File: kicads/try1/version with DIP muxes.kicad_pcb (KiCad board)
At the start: 2 copper layers, 166.5 x 100 mm, 51 parts, among them P10 CONN_01X08, P11 CONN_01X08, P12 CONN_01X08, P13 CONN_01X08, P14 CONN_01X08, P15 CONN_01X08, P16 CONN_01X08, P17 CONN_01X08, P18 CONN_01X08, P19 CONN_01X16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

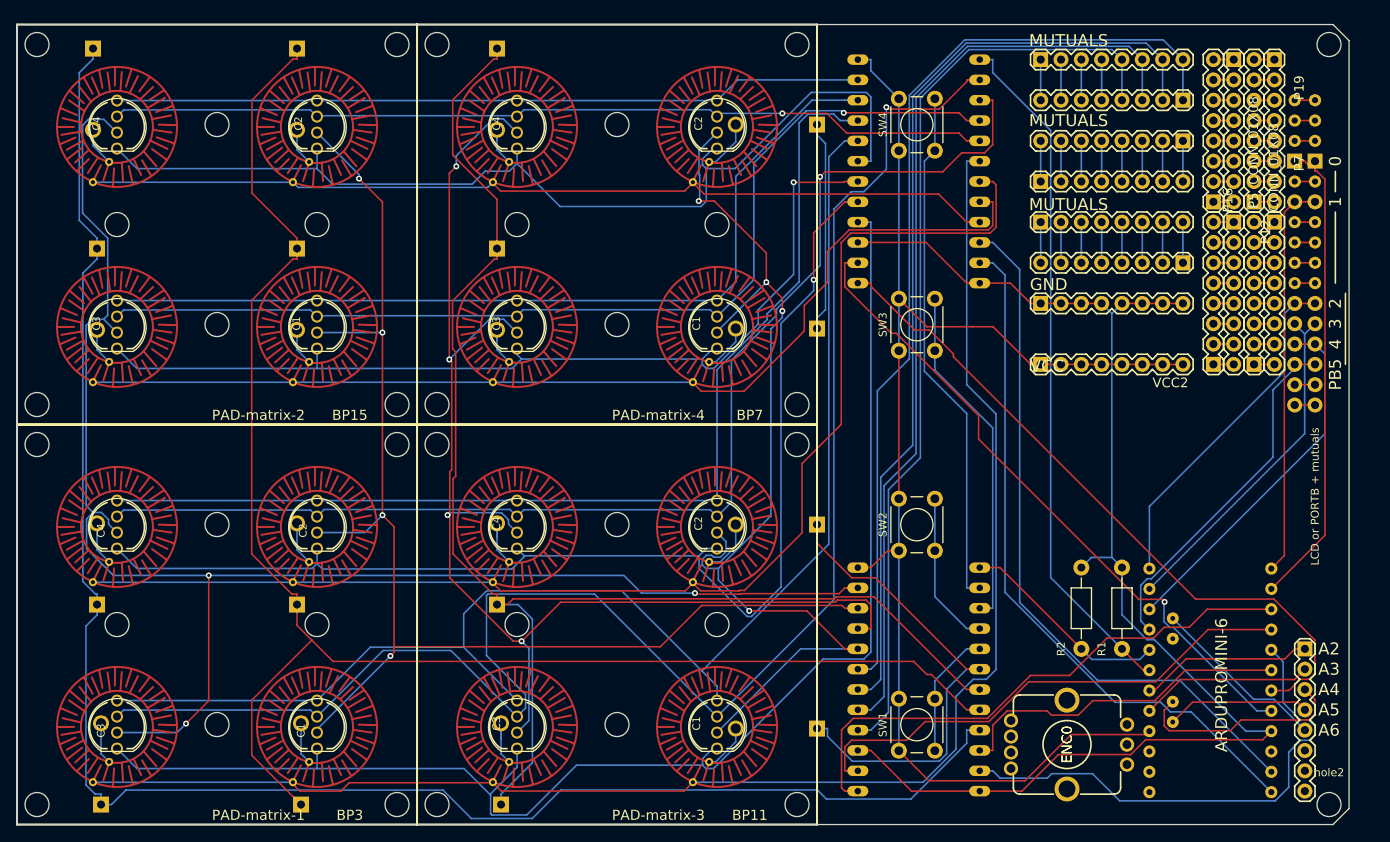
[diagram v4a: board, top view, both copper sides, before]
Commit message: starting to rollback intent to put all functionality in a library+ addition of barrel jack to pcb
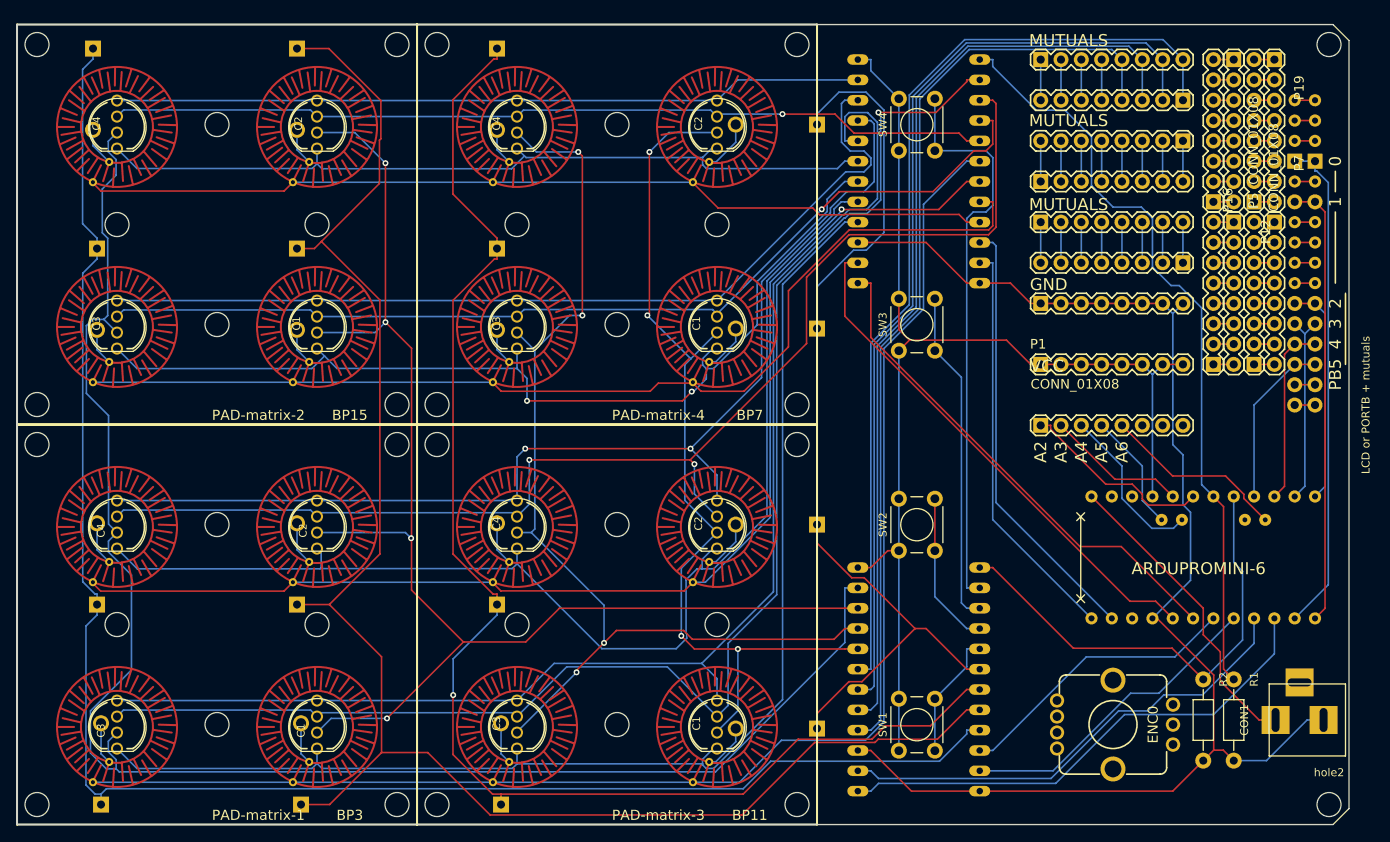
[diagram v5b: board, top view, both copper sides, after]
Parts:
- removed CONN_01X08: VCC2, SparkFun-Connectors:1X08
- added CON1: BARREL_JACK, Connect:BARREL_JACK, F.Cu at (223.5, 138.4)
- added P1: CONN_01X08, SparkFun-Connectors:1X08, F.Cu at (188.0, 94.0)
- moved P4 43.3 mm to (188.0, 101.6), turned to 0 degrees
- moved uP1 40.4 mm to (188.0, 128.3), turned to 90 degrees
- moved R2 28.5 mm to (208.3, 143.5), turned to 90 degrees
- moved R1 14.5 mm to (212.1, 133.3), turned to 270 degrees
- moved ENC0 6.27 mm to (197.0, 139.0)
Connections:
- uP1 pad 19: Net-(uP1-Pad19) -> RAWVCC
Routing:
- net RAWVCC: track 0.00 -> 38.7 mm
- net /PD1: track 87.1 -> 51.2 mm
- net /PD0: track 88.2 -> 54.8 mm
- net /A0: track 26.5 -> 59.1 mm
- net /MUXBG10: track 160.5 -> 131.6 mm
- net /MUXAB7: track 209.6 -> 181.1 mm
- net /MUXAR12: track 125.7 -> 101.8 mm
- net /PD5: track 63.4 -> 39.6 mm
- net /PD3: track 86.5 -> 63.2 mm
- net /PB5: track 44.4 -> 21.2 mm
- net /PB4: track 45.3 -> 22.6 mm
- net /VCC: track 169.8 -> 148.3 mm
- net /PB3: track 43.5 -> 24.4 mm
- net /PD2: track 83.1 -> 64.9 mm, vias 1 -> 0
- net /MUXAR15: track 176.0 -> 160.1 mm
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
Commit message: encoder activated notes for improvement of the PCB board
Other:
- board text added: "add -6n130 schematic -resistors for midi output and input -connectors for encoder"
- board text added: "arduino will be better flipped"
- board text added: "flip resistors"
- board text added: "flip side of this barrel"
- board text added: "include connector for the ftdi"
- board text added: "names in other side. screen hides names in top"
- board text added: "screen not well aligned to encoder"
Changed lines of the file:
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@@
     (area 59.233299 43.3 231.417486 154.0782)
     (thickness 1.6)
-    (drawings 27)
+    (drawings 34)
     (tracks 837)
     (zones 0)
@@
       (net 21 /VCC))
   )
+  (gr_text "flip resistors" (at 211.4 156.8) (layer Dwgs.User)
+    (effects (font (size 1.5 1.5) (thickness 0.3)))
+  )
+  (gr_text "add\n-6n130 schematic\n-resistors for midi output and input\n-connectors for encoder" (at 257.8 87.8) (layer Dwgs.User)
+    (effects (font (size 1.5 1.5) (thickness 0.3)))
+  )
+  (gr_text "include connector for the ftdi\n" (at 245 123.4) (layer Dwgs.User)
+    (effects (font (size 1.5 1.5) (thickness 0.3)))
+  )
+  (gr_text "arduino will be better flipped" (at 244.4 118.4) (layer Dwgs.User)
+    (effects (font (size 1.5 1.5) (thickness 0.3)))
+  )
+  (gr_text "names in other side. screen hides names in top\n" (at 197.4 42) (layer Dwgs.User)
+    (effects (font (size 1.5 1.5) (thickness 0.3)))
+  )
+  (gr_text "screen not well aligned to encoder\n" (at 247.8 73.6) (layer Dwgs.User)
+    (effects (font (size 1.5 1.5) (thickness 0.3)))
+  )
+  (gr_text "flip side of this barrel\n" (at 241 138.4) (layer Dwgs.User)
+    (effects (font (size 1.5 1.5) (thickness 0.3)))
+  )
   (dimension 166.5 (width 0.3) (layer B.SilkS)

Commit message: body for the v2 prorotype started additional notes on the pcb design
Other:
- board text added: "this protoboard is awkward. think that dip packs go here"
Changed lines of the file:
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@@
     (links 253)
     (no_connects 0)
-    (area 59.233299 43.3 231.417486 154.0782)
+    (area 59.233299 40.8 278.835716 158.15)
     (thickness 1.6)
-    (drawings 34)
+    (drawings 50)
     (tracks 837)
     (zones 0)
@@
     (pad_to_mask_clearance 0)
     (aux_axis_origin 0 0)
-    (visible_elements 7FFFEFFF)
+    (visible_elements 7FFFFFFF)
     (pcbplotparams
       (layerselection 0x010f0_80000001)
@@
       (net 21 /VCC))
   )
+  (dimension 8.5 (width 0.3) (layer Dwgs.User)
+    (gr_text "8,500 mm" (at 235.35 147.25 270) (layer Dwgs.User)
+      (effects (font (size 1.5 1.5) (thickness 0.3)))
+    )
+    (feature1 (pts (xy 228.5 151.5) (xy 236.7 151.5)))
+    (feature2 (pts (xy 228.5 143) (xy 236.7 143)))
+    (crossbar (pts (xy 234 143) (xy 234 151.5)))
+    (arrow1a (pts (xy 234 151.5) (xy 233.413579 150.373496)))
+    (arrow1b (pts (xy 234 151.5) (xy 234.586421 150.373496)))
+    (arrow2a (pts (xy 234 143) (xy 233.413579 144.126504)))
+    (arrow2b (pts (xy 234 143) (xy 234.586421 144.126504)))
+  )
+  (dimension 12.5 (width 0.3) (layer Dwgs.User)
+    (gr_text "12,500 mm" (at 186.35 145.25 270) (layer Dwgs.User)
+      (effects (font (size 1.5 1.5) (thickness 0.3)))
+    )
+    (feature1 (pts (xy 183 151.5) (xy 187.7 151.5)))
+    (feature2 (pts (xy 183 139) (xy 187.7 139)))
+    (crossbar (pts (xy 185 139) (xy 185 151.5)))
+    (arrow1a (pts (xy 185 151.5) (xy 184.413579 150.373496)))
+    (arrow1b (pts (xy 185 151.5) (xy 185.586421 150.373496)))
+    (arrow2a (pts (xy 185 139) (xy 184.413579 140.126504)))
+    (arrow2b (pts (xy 185 139) (xy 185.586421 140.126504)))
+  )
+  (dimension 25 (width 0.3) (layer Dwgs.User)
+    (gr_text "25,000 mm" (at 186.35 126.5 270) (layer Dwgs.User)
+      (effects (font (size 1.5 1.5) (thickness 0.3)))
+    )
+    (feature1 (pts (xy 183 139) (xy 187.7 139)))
+    (feature2 (pts (xy 183 114) (xy 187.7 114)))
+    (crossbar (pts (xy 185 114) (xy 185 139)))
+    (arrow1a (pts (xy 185 139) (xy 184.413579 137.873496)))
+    (arrow1b (pts (xy 185 139) (xy 185.586421 137.873496)))
+    (arrow2a (pts (xy 185 114) (xy 184.413579 115.126504)))
+    (arrow2b (pts (xy 185 114) (xy 185.586421 115.126504)))
+  )
+  (dimension 25 (width 0.3) (layer Dwgs.User)
+    (gr_text "25,000 mm" (at 186.35 101.5 270) (layer Dwgs.User)
+      (effects (font (size 1.5 1.5) (thickness 0.3)))
+    )
+    (feature1 (pts (xy 183 114) (xy 187.7 114)))
+    (feature2 (pts (xy 183 89) (xy 187.7 89)))
+    (crossbar (pts (xy 185 89) (xy 185 114)))
+    (arrow1a (pts (xy 185 114) (xy 184.413579 112.873496)))
+    (arrow1b (pts (xy 185 114) (xy 185.586421 112.873496)))
+    (arrow2a (pts (xy 185 89) (xy 184.413579 90.126504)))
+    (arrow2b (pts (xy 185 89) (xy 185.586421 90.126504)))
+  )
+  (dimension 25 (width 0.3) (layer Dwgs.User)
+    (gr_text "25,000 mm" (at 186.35 76.5 270) (layer Dwgs.User)
+      (effects (font (size 1.5 1.5) (thickness 0.3)))
+    )
+    (feature1 (pts (xy 183 89) (xy 187.7 89)))
+    (feature2 (pts (xy 183 64) (xy 187.7 64)))
+    (crossbar (pts (xy 185 64) (xy 185 89)))
+    (arrow1a (pts (xy 185 89) (xy 184.413579 87.873496)))
+    (arrow1b (pts (xy 185 89) (xy 185.586421 87.873496)))
+    (arrow2a (pts (xy 185 64) (xy 184.413579 65.126504)))
+    (arrow2b (pts (xy 185 64) (xy 185.586421 65.126504)))
+  )
+  (dimension 12.5 (width 0.3) (layer Dwgs.User)
+    (gr_text "12,500 mm" (at 185.85 57.75 90) (layer Dwgs.User)
+      (effects (font (size 1.5 1.5) (thickness 0.3)))
+    )
+    (feature1 (pts (xy 183 51.5) (xy 187.2 51.5)))
+    (feature2 (pts (xy 183 64) (xy 187.2 64)))
+    (crossbar (pts (xy 184.5 64) (xy 184.5 51.5)))
+    (arrow1a (pts (xy 184.5 51.5) (xy 185.086421 52.626504)))
+    (arrow1b (pts (xy 184.5 51.5) (xy 183.913579 52.626504)))
+    (arrow2a (pts (xy 184.5 64) (xy 185.086421 62.873496)))
+    (arrow2b (pts (xy 184.5 64) (xy 183.913579 62.873496)))
+  )
+  (dimension 12.5 (width 0.3) (layer Dwgs.User)
+    (gr_text "12,500 mm" (at 193.150001 145.25 270) (layer Dwgs.User)
+      (effects (font (size 1.5 1.5) (thickness 0.3)))
+    )
+    (feature1 (pts (xy 197 151.5) (xy 191.800001 151.5)))
+    (feature2 (pts (xy 197 139) (xy 191.800001 139)))
+    (crossbar (pts (xy 194.500001 139) (xy 194.500001 151.5)))
+    (arrow1a (pts (xy 194.500001 151.5) (xy 193.91358 150.373496)))
+    (arrow1b (pts (xy 194.500001 151.5) (xy 195.086422 150.373496)))
+    (arrow2a (pts (xy 194.500001 139) (xy 193.91358 140.126504)))
+    (arrow2b (pts (xy 194.500001 139) (xy 195.086422 140.126504)))
+  )
+  (gr_text "this protoboard is awkward. think that dip packs go here" (at 215.5 49) (layer Dwgs.User)
+    (effects (font (size 1.5 1.5) (thickness 0.3)))
+  )
+  (dimension 24.5 (width 0.3) (layer Dwgs.User)
+    (gr_text "24,500 mm" (at 184.75 163.35) (layer Dwgs.User)
+      (effects (font (size 1.5 1.5) (thickness 0.3)))
+    )
+    (feature1 (pts (xy 197 139) (xy 197 164.7)))
+    (feature2 (pts (xy 172.5 139) (xy 172.5 164.7)))
+    (crossbar (pts (xy 172.5 162) (xy 197 162)))
+    (arrow1a (pts (xy 197 162) (xy 195.873496 162.586421)))
+    (arrow1b (pts (xy 197 162) (xy 195.873496 161.413579)))
+    (arrow2a (pts (xy 172.5 162) (xy 173.626504 162.586421)))
+    (arrow2b (pts (xy 172.5 162) (xy 173.626504 161.413579)))
+  )
+  (dimension 29.5 (width 0.3) (layer Dwgs.User)
+    (gr_text "29,500 mm" (at 211.75 163.35) (layer Dwgs.User)
+      (effects (font (size 1.5 1.5) (thickness 0.3)))
+    )
+    (feature1 (pts (xy 226.5 139) (xy 226.5 164.7)))
+    (feature2 (pts (xy 197 139) (xy 197 164.7)))
+    (crossbar (pts (xy 197 162) (xy 226.5 162)))
+    (arrow1a (pts (xy 226.5 162) (xy 225.373496 162.586421)))
+    (arrow1b (pts (xy 226.5 162) (xy 225.373496 161.413579)))
+    (arrow2a (pts (xy 197 162) (xy 198.126504 162.586421)))
+    (arrow2b (pts (xy 197 162) (xy 198.126504 161.413579)))
+  )
+  (dimension 161.5 (width 0.3) (layer Dwgs.User)
+    (gr_text "161,500 mm" (at 143.25 31.650001) (layer Dwgs.User)
+      (effects (font (size 1.5 1.5) (thickness 0.3)))
+    )
+    (feature1 (pts (xy 62.5 54) (xy 62.5 30.300001)))
+    (feature2 (pts (xy 224 54) (xy 224 30.300001)))
+    (crossbar (pts (xy 224 33.000001) (xy 62.5 33.000001)))
+    (arrow1a (pts (xy 62.5 33.000001) (xy 63.626504 32.41358)))
+    (arrow1b (pts (xy 62.5 33.000001) (xy 63.626504 33.586422)))
+    (arrow2a (pts (xy 224 33.000001) (xy 222.873496 32.41358)))
+    (arrow2b (pts (xy 224 33.000001) (xy 222.873496 33.586422)))
+  )
+  (dimension 45 (width 0.3) (layer Dwgs.User)
+    (gr_text "45,000 mm" (at 54.650001 76.5 270) (layer Dwgs.User)
+      (effects (font (size 1.5 1.5) (thickness 0.3)))
+    )
+    (feature1 (pts (xy 62.5 99) (xy 53.300001 99)))
+    (feature2 (pts (xy 62.5 54) (xy 53.300001 54)))
+    (crossbar (pts (xy 56.000001 54) (xy 56.000001 99)))
+    (arrow1a (pts (xy 56.000001 99) (xy 55.41358 97.873496)))
+    (arrow1b (pts (xy 56.000001 99) (xy 56.586422 97.873496)))
+    (arrow2a (pts (xy 56.000001 54) (xy 55.41358 55.126504)))
+    (arrow2b (pts (xy 56.000001 54) (xy 56.586422 55.126504)))
+  )
+  (dimension 100 (width 0.3) (layer Dwgs.User)
+    (gr_text "100,000 mm" (at 34.650001 101.5 270) (layer Dwgs.User)
+      (effects (font (size 1.5 1.5) (thickness 0.3)))
+    )
+    (feature1 (pts (xy 60 151.5) (xy 33.300001 151.5)))
+    (feature2 (pts (xy 60 51.5) (xy 33.300001 51.5)))
+    (crossbar (pts (xy 36.000001 51.5) (xy 36.000001 151.5)))
+    (arrow1a (pts (xy 36.000001 151.5) (xy 35.41358 150.373496)))
+    (arrow1b (pts (xy 36.000001 151.5) (xy 36.586422 150.373496)))
+    (arrow2a (pts (xy 36.000001 51.5) (xy 35.41358 52.626504)))
+    (arrow2b (pts (xy 36.000001 51.5) (xy 36.586422 52.626504)))
+  )
+  (dimension 95 (width 0.3) (layer Dwgs.User)
+    (gr_text "95,000 mm" (at 49.025001 101.5 270) (layer Dwgs.User)
+      (effects (font (size 1.5 1.5) (thickness 0.3)))
+    )
+    (feature1 (pts (xy 62.5 149) (xy 47.675001 149)))
+    (feature2 (pts (xy 62.5 54) (xy 47.675001 54)))
+    (crossbar (pts (xy 50.375001 54) (xy 50.375001 149)))
+    (arrow1a (pts (xy 50.375001 149) (xy 49.78858 147.873496)))
+    (arrow1b (pts (xy 50.375001 149) (xy 50.961422 147.873496)))
+    (arrow2a (pts (xy 50.375001 54) (xy 49.78858 55.126504)))
+    (arrow2b (pts (xy 50.375001 54) (xy 50.961422 55.126504)))
+  )
+  (dimension 45 (width 0.3) (layer Dwgs.User)
+    (gr_text "45,000 mm" (at 85 43.525) (layer Dwgs.User)
+      (effects (font (size 1.5 1.5) (thickness 0.3)))
+    )
+    (feature1 (pts (xy 107.5 54) (xy 107.5 42.175)))
+    (feature2 (pts (xy 62.5 54) (xy 62.5 42.175)))
+    (crossbar (pts (xy 62.5 44.875) (xy 107.5 44.875)))
+    (arrow1a (pts (xy 107.5 44.875) (xy 106.373496 45.461421)))
+    (arrow1b (pts (xy 107.5 44.875) (xy 106.373496 44.288579)))
+    (arrow2a (pts (xy 62.5 44.875) (xy 63.626504 45.461421)))
+    (arrow2b (pts (xy 62.5 44.875) (xy 63.626504 44.288579)))
+  )
+  (dimension 95 (width 0.3) (layer Dwgs.User)
+    (gr_text "95,000 mm" (at 110 40.175) (layer Dwgs.User)
+      (effects (font (size 1.5 1.5) (thickness 0.3)))
+    )
+    (feature1 (pts (xy 157.5 54) (xy 157.5 38.825)))
+    (feature2 (pts (xy 62.5 54) (xy 62.5 38.825)))
+    (crossbar (pts (xy 62.5 41.525) (xy 157.5 41.525)))
+    (arrow1a (pts (xy 157.5 41.525) (xy 156.373496 42.111421)))
+    (arrow1b (pts (xy 157.5 41.525) (xy 156.373496 40.938579)))
+    (arrow2a (pts (xy 62.5 41.525) (xy 63.626504 42.111421)))
+    (arrow2b (pts (xy 62.5 41.525) (xy 63.626504 40.938579)))
+  )
   (gr_text "flip resistors" (at 211.4 156.8) (layer Dwgs.User)

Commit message: notes on pcb
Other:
- board text added: "free serial ports, you dumb"
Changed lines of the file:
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@@
     (links 253)
     (no_connects 0)
-    (area 59.233299 40.8 278.835716 158.15)
+    (area 27.435717 30.300001 278.835716 164.700001)
     (thickness 1.6)
-    (drawings 50)
+    (drawings 51)
     (tracks 837)
     (zones 0)
@@
     (pad_to_mask_clearance 0)
     (aux_axis_origin 0 0)
-    (visible_elements 7FFFFFFF)
+    (visible_elements 7FFFEFFF)
     (pcbplotparams
       (layerselection 0x010f0_80000001)
@@
       (net 21 /VCC))
   )
+  (gr_text "free serial ports, you dumb" (at 205 115) (layer Dwgs.User)
+    (effects (font (size 1.5 1.5) (thickness 0.3)))
+  )
   (dimension 8.5 (width 0.3) (layer Dwgs.User)
